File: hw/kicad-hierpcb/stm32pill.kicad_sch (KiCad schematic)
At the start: 53 parts, among them SW1 Tactile Switch, SW2 Tactile Switch, U1 3.3V Voltage Regulator 200mA, X1 Crystal 12MHz X322512MSB4SI

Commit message: added capacitor at volatage regulator input
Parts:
- added CUin1: 1μF, jlcpcb:C0402, symbol jlcpcb:Capacitor 1μF 0402 CL05A105KA5NQNC
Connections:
- net GND: now also CUin1.2
- net VBUS: now also CUin1.1
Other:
- moved on the sheet: RVbusI1, RVbusO1
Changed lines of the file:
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@@
 	)
 	(junction
+		(at 62.23 45.72)
+		(diameter 0)
+		(color 0 0 0 0)
+	)
+	(junction
 		(at 26.67 118.11)
 		(diameter 0)
@@
 	)
 	(junction
-		(at 93.98 36.83)
+		(at 62.23 24.13)
 		(diameter 0)
 		(color 0 0 0 0)
 	)
 	(junction
-		(at 97.79 67.31)
+		(at 93.98 36.83)
 		(diameter 0)
 		(color 0 0 0 0)
 	)
 	(junction
-		(at 269.24 85.09)
+		(at 97.79 67.31)
 		(diameter 0)
 		(color 0 0 0 0)
 	)
 	(junction
-		(at 114.3 130.81)
+		(at 269.24 85.09)
 		(diameter 0)
 		(color 0 0 0 0)
 	)
 	(junction
-		(at 55.88 24.13)
+		(at 114.3 130.81)
 		(diameter 0)
 		(color 0 0 0 0)
@@
 	)
 	(junction
-		(at 55.88 34.29)
+		(at 62.23 34.29)
 		(diameter 0)
 		(color 0 0 0 0)
@@
 	(wire
 		(pts
-			(xy 66.04 34.29) (xy 69.85 34.29)
-		)
-		(stroke
-			(width 0)
-			(type default)
-		)
-	)
-	(wire
-		(pts
 			(xy 80.01 139.7) (xy 82.55 139.7)
 		)
@@
 	(wire
 		(pts
+			(xy 62.23 45.72) (xy 62.23 44.45)
+		)
+		(stroke
+			(width 0)
+			(type default)
+		)
+	)
+	(wire
+		(pts
 			(xy 80.01 80.01) (xy 118.11 80.01)
 		)
@@
 	(wire
 		(pts
-			(xy 55.88 24.13) (xy 49.53 24.13)
+			(xy 49.53 24.13) (xy 62.23 24.13)
 		)
 		(stroke
@@
 	(wire
 		(pts
+			(xy 66.04 34.29) (xy 72.39 34.29)
+		)
+		(stroke
+			(width 0)
+			(type default)
+		)
+	)
+	(wire
+		(pts
 			(xy 161.29 115.57) (xy 219.71 115.57)
 		)
@@
 	(wire
 		(pts
-			(xy 66.04 34.29) (xy 55.88 34.29)
+			(xy 49.53 45.72) (xy 62.23 45.72)
 		)
 		(stroke
@@
 	(wire
 		(pts
+			(xy 49.53 43.18) (xy 49.53 45.72)
+		)
+		(stroke
+			(width 0)
+			(type default)
+		)
+	)
+	(wire
+		(pts
 			(xy 53.34 95.25) (xy 58.42 95.25)
 		)
@@
 	(wire
 		(pts
-			(xy 49.53 29.21) (xy 49.53 30.48)
+			(xy 49.53 29.21) (xy 49.53 33.02)
 		)
 		(stroke
@@
 	(wire
 		(pts
+			(xy 62.23 24.13) (xy 66.04 24.13)
+		)
+		(stroke
+			(width 0)
+			(type default)
+		)
+	)
+	(wire
+		(pts
 			(xy 82.55 31.75) (xy 90.17 31.75)
 		)
@@
 	(wire
 		(pts
+			(xy 62.23 46.99) (xy 62.23 45.72)
+		)
+		(stroke
+			(width 0)
+			(type default)
+		)
+	)
+	(wire
+		(pts
 			(xy 129.54 39.37) (xy 113.03 39.37)
 		)
@@
 	(wire
 		(pts
-			(xy 105.41 29.21) (xy 129.54 29.21)
+			(xy 66.04 34.29) (xy 62.23 34.29)
 		)
 		(stroke
@@
 	(wire
 		(pts
-			(xy 49.53 24.13) (xy 49.53 29.21)
+			(xy 105.41 29.21) (xy 129.54 29.21)
 		)
 		(stroke
@@
 	(wire
 		(pts
-			(xy 46.99 115.57) (xy 118.11 115.57)
+			(xy 49.53 24.13) (xy 49.53 29.21)
 		)
 		(stroke
@@
 	(wire
 		(pts
-			(xy 198.12 66.04) (xy 198.12 85.09)
+			(xy 46.99 115.57) (xy 118.11 115.57)
 		)
 		(stroke
@@
 	(wire
 		(pts
-			(xy 26.67 87.63) (xy 29.21 87.63)
+			(xy 198.12 66.04) (xy 198.12 85.09)
 		)
 		(stroke
@@
 	(wire
 		(pts
-			(xy 269.24 95.25) (xy 254 95.25)
+			(xy 26.67 87.63) (xy 29.21 87.63)
 		)
 		(stroke
@@
 	(wire
 		(pts
-			(xy 69.85 85.09) (xy 118.11 85.09)
+			(xy 269.24 95.25) (xy 254 95.25)
 		)
 		(stroke
@@
 	(wire
 		(pts
-			(xy 161.29 85.09) (xy 198.12 85.09)
+			(xy 69.85 85.09) (xy 118.11 85.09)
 		)
 		(stroke
@@
 	(wire
 		(pts
-			(xy 55.88 24.13) (xy 66.04 24.13)
+			(xy 161.29 85.09) (xy 198.12 85.09)
 		)
 		(stroke
@@
 		)
 	)
-	(hierarchical_label "VBUS"
-		(shape input)
-		(at 49.53 30.48 270)
-		(fields_autoplaced yes)
-		(effects
-			(font
-				(size 1.27 1.27)
-			)
-			(justify right)
-		)
-	)
 	(hierarchical_label "VBAT"
 		(shape input)
@@
 		)
 	)
+	(hierarchical_label "VBUS"
+		(shape input)
+		(at 49.53 29.21 0)
+		(fields_autoplaced yes)
+		(effects
+			(font
+				(size 1.27 1.27)
+			)
+			(justify left)
+		)
+	)
 	(hierarchical_label "USBd+"
 		(shape input)
@@
 	(symbol
 		(lib_id "jlcpcb:Resistor 51kΩ 0402WGF5102TCE")
-		(at 55.88 29.21 270)
+		(at 62.23 29.21 270)
 		(unit 1)
 		(exclude_from_sim no)
@@
 		(dnp no)
 		(property "Reference" "RVbusI1"
-			(at 57.658 27.94 90)
+			(at 64.77 26.162 0)
 			(effects
 				(font
@@
 		)
 		(property "Value" "51kΩ"
-			(at 53.086 30.226 0)
+			(at 59.436 30.226 0)
 			(effects
 				(font
@@
 		)
 		(property "Footprint" "jlcpcb:R0402"
-			(at 48.26 29.21 0)
+			(at 54.61 29.21 0)
 			(effects
 				(font
@@
 		)
 		(property "Datasheet" "https://lcsc.com/product-detail/Chip-Resistor-Surface-Mount-UniOhm_51KR-5102-1_C25794.html"
-			(at 45.72 29.21 0)
+			(at 52.07 29.21 0)
 			(effects
 				(font
@@
 		)
 		(property "Description" ""
-			(at 55.88 29.21 0)
+			(at 62.23 29.21 0)
 			(effects
 				(font
@@
 		)
 		(property "LCSC Part" "C25794"
-			(at 43.18 29.21 0)
+			(at 49.53 29.21 0)
 			(effects
 				(font
@@
 	(symbol
 		(lib_id "power:GND")
-		(at 55.88 44.45 0)
+		(at 62.23 46.99 0)
 		(unit 1)
 		(exclude_from_sim no)
@@
 		(fields_autoplaced yes)
 		(property "Reference" "#PWR06"
-			(at 55.88 50.8 0)
+			(at 62.23 53.34 0)
 			(effects
 				(font
@@
 		)
 		(property "Value" "GND"
-			(at 55.88 49.53 0)
+			(at 62.23 52.07 0)
 			(effects
 				(font
@@
 		)
 		(property "Footprint" ""
-			(at 55.88 44.45 0)
+			(at 62.23 46.99 0)
 			(effects
 				(font
@@
 		)
 		(property "Datasheet" ""
-			(at 55.88 44.45 0)
+			(at 62.23 46.99 0)
 			(effects
 				(font
@@
 		)
 		(property "Description" "Power symbol creates a global label with name \"GND\" , ground"
-			(at 55.88 44.45 0)
+			(at 62.23 46.99 0)
 			(effects
 				(font
@@
 	)
 	(symbol
+		(lib_id "jlcpcb:Capacitor 1μF 0402 CL05A105KA5NQNC")
+		(at 49.53 38.1 270)
+		(unit 1)
+		(exclude_from_sim no)
+		(in_bom yes)
+		(on_board yes)
+		(dnp no)
+		(property "Reference" "CUin1"
+			(at 46.482 36.322 0)
+			(effects
+				(font
+					(size 1.27 1.27)
+				)
+				(justify left)
+			)
+		)
+		(property "Value" "1μF"
+			(at 52.07 37.846 90)
+			(effects
+				(font
+					(size 1.27 1.27)
+				)
+				(justify left)
+			)
+		)
+		(property "Footprint" "jlcpcb:C0402"
+			(at 41.91 38.1 0)
+			(effects
+				(font
+					(size 1.27 1.27)
+				)
+				(hide yes)
+			)
+		)
+		(property "Datasheet" "https://lcsc.com/product-detail/Multilayer-Ceramic-Capacitors-MLCC-SMD-SMT_SAMSUNG_CL05A105KA5NQNC_1uF-105-10-25V_C52923.html"
+			(at 39.37 38.1 0)
+			(effects
+				(font
+					(size 1.27 1.27)
+				)
+				(hide yes)
+			)
+		)
+		(property "Description" ""
+			(at 49.53 38.1 0)
+			(effects
+				(font
+					(size 1.27 1.27)
+				)
+				(hide yes)
+			)
+		)
+		(property "LCSC Part" "C52923"
+			(at 36.83 38.1 0)
+			(effects
+				(font
+					(size 1.27 1.27)
+				)
+				(hide yes)
+			)
+		)
+		(pin "1"
+		)
+		(pin "2"
+		)
+		(instances
+			(project ""
+				(path "/02648bdf-775f-4db3-b3af-d1ac51708c5a"
+					(reference "CUin1")
+					(unit 1)
+				)
+			)
+		)
+	)
+	(symbol
 		(lib_id "power:GND")
 		(at 105.41 39.37 0)
@@
 	(symbol
 		(lib_id "jlcpcb:Resistor 100kΩ 0402WGF1003TCE")
-		(at 55.88 39.37 270)
+		(at 62.23 39.37 270)
 		(unit 1)
 		(exclude_from_sim no)
@@
 		(dnp no)
 		(property "Reference" "RVbusO1"
-			(at 57.658 38.1 90)
+			(at 64.516 36.576 0)
 			(effects
 				(font
@@
 		)
 		(property "Value" "100kΩ"
-			(at 53.34 39.878 0)
+			(at 59.69 39.878 0)
 			(effects
 				(font
@@
 		)
 		(property "Footprint" "jlcpcb:R0402"
-			(at 48.26 39.37 0)
+			(at 54.61 39.37 0)
 			(effects
 				(font
@@
 		)
 		(property "Datasheet" "https://lcsc.com/product-detail/Chip-Resistor-Surface-Mount-UniOhm_100KR-1003-1_C25741.html"
-			(at 45.72 39.37 0)
+			(at 52.07 39.37 0)
 			(effects
 				(font
@@
 		)
 		(property "Description" ""
-			(at 55.88 39.37 0)
+			(at 62.23 39.37 0)
 			(effects
 				(font
@@
 		)
 		(property "LCSC Part" "C25741"
-			(at 43.18 39.37 0)
+			(at 49.53 39.37 0)
 			(effects
 				(font

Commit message: improved layout
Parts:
- removed JPV1: SolderJumper_2_Open, Jumper:SolderJumper-2_P1.3mm_Open_RoundedPad1.0x1.5mm, symbol Jumper:SolderJumper_2_Open
- removed VSSA1: VSSA, TestPoint:TestPoint_THTPad_D1.0mm_Drill0.5mm, symbol Connector:Conn_01x01_Pin
- added CC1_1, CC2_1, SBU1_1, SBU2_1: ~, base:TestPoint_THTPad_D1.0mm_Drill0.5mm, symbol Connector:Conn_01x01_Pin
- added CLed1: 100nF, jlcpcb:C0402, symbol jlcpcb:Capacitor 100nF 4002 CL05B104KO5NNNC
- added CUout1: 1μF, jlcpcb:C0402, symbol jlcpcb:Capacitor 1μF 0402 CL05A105KA5NQNC
- added DO1: ~, base:PTH 1.7mm, symbol Connector:Conn_01x01_Pin
- added JPV1: SolderJumper_3_Open, Jumper:SolderJumper-3_P1.3mm_Open_RoundedPad1.0x1.5mm, symbol Jumper:SolderJumper_3_Open
- added RGB1: LED WS2812B, jlcpcb:LED-SMD_4P-L5.0-W5.0-TL-1, symbol jlcpcb:LED WS2812B-S XL-5050RGBC
- JVbat1: footprint TestPoint:TestPoint_THTPad_D1.0mm_Drill0.5mm -> base:TestPoint_THTPad_D1.0mm_Drill0.5mm
- RGB2: renamed from RGB1; value LED WS2812B-S XL-5050RGBC -> LED WS2812B
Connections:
- net +3.3V: now also CVcc1.1, CLed1.2, JPV1.2 (C), RGB1.1 (VDD); no longer CVcc1.2, U1.3 (Vout)
- net GND: now also CVcc1.2, CLed1.1, CUout1.2, RGB1.3 (GND); no longer CVcc1.1
- net I2C1 SCL: now also IDE_STM_D1.SCL (IDE39_STM45); no longer IDE_STM_D1.SDA (IDE39_STM45)
- net I2C1 SDA: now also IDE_STM_D1.SDA (IDE37_STM46); no longer IDE_STM_D1.SCL (IDE37_STM46)
- net at IDE_STM_C1.3V3 (IDE1_STM23): now also JPV1.3 (B)
- net at DI1.1 (Pin_1): now also RGB1.4 (DI); no longer RGB2.4 (DI)
- net at RGB2.2 (DO): now also DO1.1 (Pin_1)
- net CC1: now reaches USB1.A5 (CC1)
- net CC1: now also CC1_1.1 (Pin_1)
- net SBU1: now reaches USB1.A8 (SBU1)
- net SBU1: now also SBU1_1.1 (Pin_1)
- net CC2: now reaches USB1.B5 (CC2)
- net CC2: now also CC2_1.1 (Pin_1)
- net SBU2: now reaches USB1.B8 (SBU2)
- net SBU2: now also SBU2_1.1 (Pin_1)
- new net: CUout1.1, JPV1.1 (A), U1.3 (Vout)
- new net: RGB1.2 (DO), RGB2.4 (DI)
- no-connect marks 11 -> 6
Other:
- moved on the sheet: JPpuUSB1, JPpuUSBconst1, JpuUSB1, L1, RGB2, RVbusI1, RVbusO1, RpuUSB1, U1

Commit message: annotations
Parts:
- added VBus_1: ~, base:TestPoint_THTPad_D1.0mm_Drill0.5mm, symbol Connector:Conn_01x01_Pin
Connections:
- net at L1.2, USB1.A4 (VBUS), USB1.A9 (VBUS)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: now also VBus_1.1 (Pin_1)
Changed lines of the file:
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@@
 	)
 	(junction
+		(at 105.41 24.13)
+		(diameter 0)
+		(color 0 0 0 0)
+	)
+	(junction
 		(at 271.78 134.62)
 		(diameter 0)
@@
 	(wire
 		(pts
+			(xy 105.41 24.13) (xy 107.95 24.13)
+		)
+		(stroke
+			(width 0)
+			(type default)
+		)
+	)
+	(wire
+		(pts
 			(xy 90.17 72.39) (xy 118.11 72.39)
 		)
@@
 	(wire
 		(pts
+			(xy 128.27 15.24) (xy 107.95 15.24)
+		)
+		(stroke
+			(width 0)
+			(type default)
+		)
+	)
+	(wire
+		(pts
 			(xy 214.63 138.43) (xy 191.77 138.43)
 		)
@@
 	(wire
 		(pts
+			(xy 107.95 15.24) (xy 107.95 24.13)
+		)
+		(stroke
+			(width 0)
+			(type default)
+		)
+	)
+	(wire
+		(pts
 			(xy 26.67 129.54) (xy 80.01 129.54)
 		)
@@
 					(unit 1)
 				)
+			)
+		)
+	)
+	(symbol
+		(lib_id "Connector:Conn_01x01_Pin")
+		(at 133.35 15.24 0)
+		(mirror y)
+		(unit 1)
+		(exclude_from_sim no)
+		(in_bom yes)
+		(on_board yes)
+		(dnp no)
+		(property "Reference" "VBus_1"
+			(at 139.7 15.24 0)
+			(effects
+				(font
+					(size 1.27 1.27)
+				)
+			)
+		)
+		(property "Value" "~"
+			(at 132.715 12.7 0)
+			(effects
+				(font
+					(size 1.27 1.27)
+				)
+				(hide yes)
+			)
+		)
+		(property "Footprint" "base:TestPoint_THTPad_D1.0mm_Drill0.5mm"
+			(at 133.35 15.24 0)
+			(effects
+				(font
+					(size 1.27 1.27)
+				)
+				(hide yes)
+			)
+		)
+		(property "Datasheet" "~"
+			(at 133.35 15.24 0)
+			(effects
+				(font
+					(size 1.27 1.27)
+				)
+				(hide yes)
+			)
+		)
+		(property "Description" "Generic connector, single row, 01x01, script generated"
+			(at 133.35 15.24 0)
+			(effects
+				(font
+					(size 1.27 1.27)
+				)
+				(hide yes)
+			)
+		)
+		(pin "1"
+		)
+		(instances
+			(project "stm32pill"
+				(path "/02648bdf-775f-4db3-b3af-d1ac51708c5a"
+					(reference "VBus_1")
+					(unit 1)
+				)

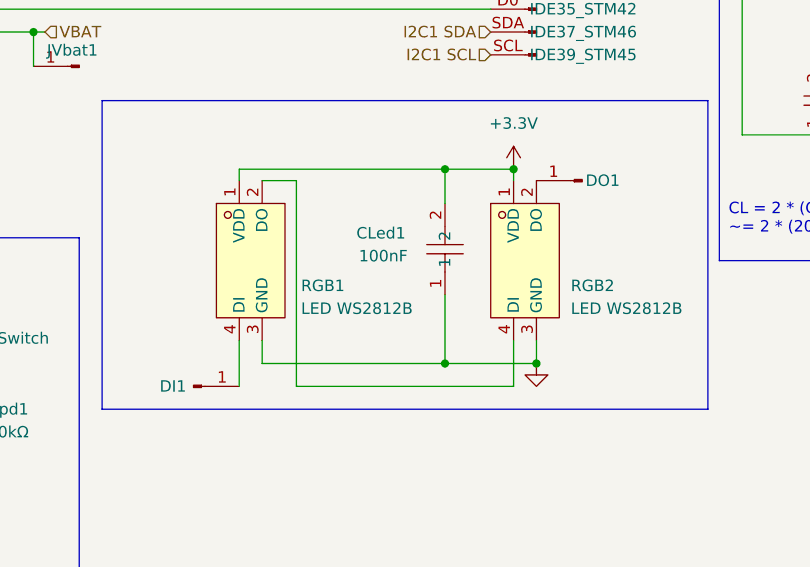
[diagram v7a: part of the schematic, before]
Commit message: changed layout of bus board
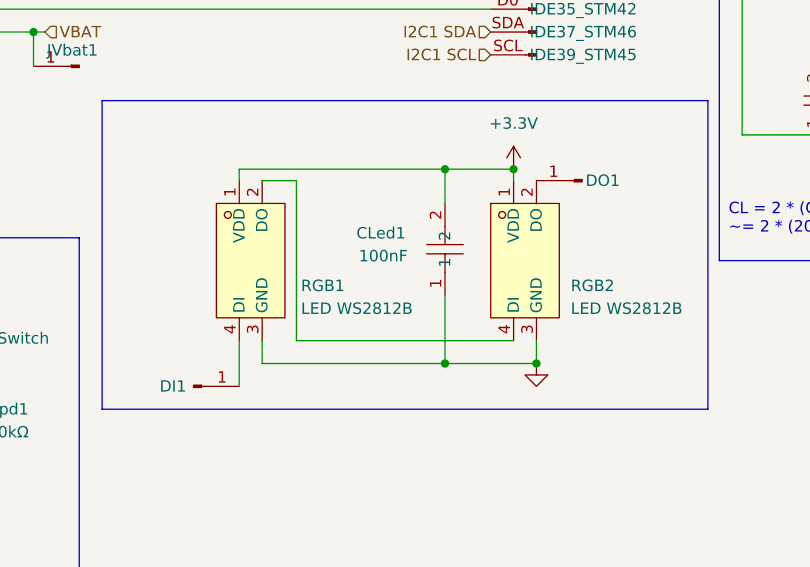
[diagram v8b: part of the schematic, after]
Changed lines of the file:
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@@
 	(wire
 		(pts
-			(xy 222.25 162.56) (xy 198.12 162.56)
+			(xy 222.25 157.48) (xy 198.12 157.48)
 		)
 		(stroke
@@
 	(wire
 		(pts
-			(xy 222.25 157.48) (xy 222.25 162.56)
-		)
-		(stroke
-			(width 0)
-			(type default)
-		)
-	)
-	(wire
-		(pts
 			(xy 214.63 69.85) (xy 219.71 69.85)
 		)
@@
 	(wire
 		(pts
-			(xy 198.12 162.56) (xy 198.12 139.7)
-		)
-		(stroke
+			(xy 198.12 157.48) (xy 198.12 139.7)
+		)
+		(stroke
